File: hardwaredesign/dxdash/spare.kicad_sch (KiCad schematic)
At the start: 0 parts

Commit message: added screw terminals
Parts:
- added J10, J11, J3, J7, J9: Screw_Terminal_01x04, TerminalBlock_Phoenix:TerminalBlock_Phoenix_MKDS-3-4-5.08_1x04_P5.08mm_Horizontal, symbol Connector:Screw_Terminal_01x04
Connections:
- new net 24V: J3.1 (Pin_1)
- new net CANH: J9.1 (Pin_1)
- new net CANL: J9.2 (Pin_2)
- new net GND: J10.1 (Pin_1), J3.2 (Pin_2)
- new net OUT1_LS: J3.3 (Pin_3)
- new net OUT2_LS: J3.4 (Pin_4)
- new net OUT3_LS: J7.1 (Pin_1)
- new net button1: J11.1 (Pin_1)
- new net button2: J11.2 (Pin_2)
- new net button3: J11.3 (Pin_3)
- new net button4: J11.4 (Pin_4)
- new net pot1: J10.2 (Pin_2)
- new net pot2: J10.3 (Pin_3)
- new net pot5V: J10.4 (Pin_4)
- no-connect marks 0 -> 5

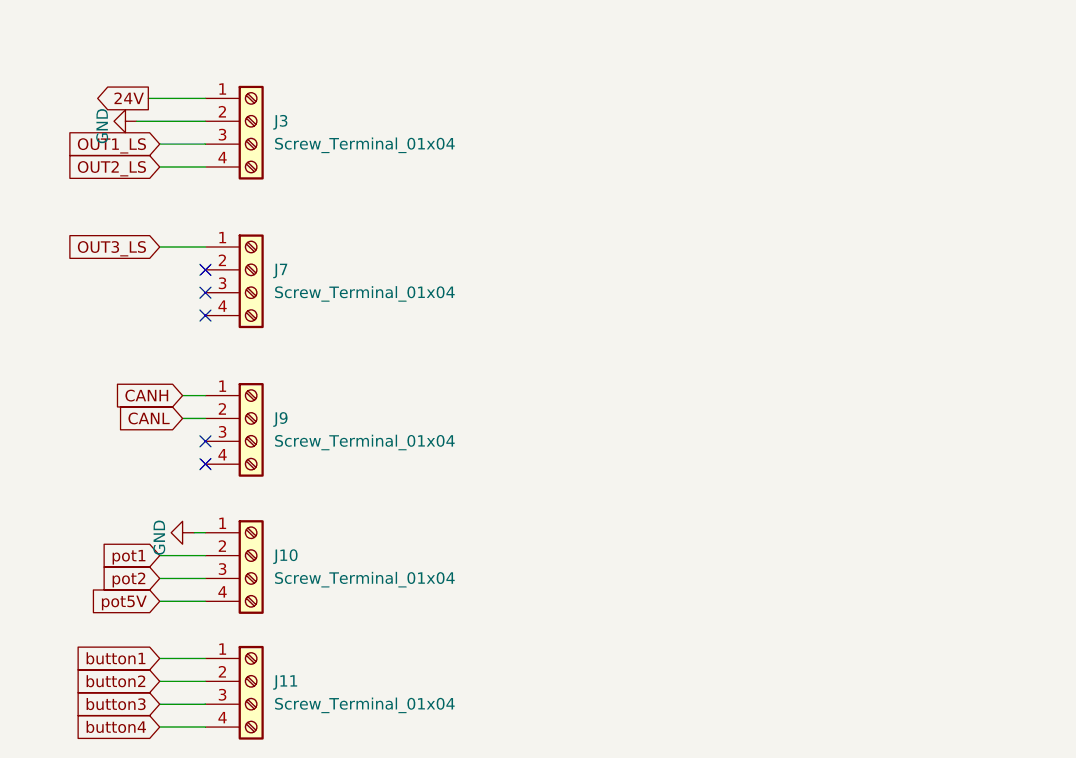
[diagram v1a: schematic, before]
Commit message: added switch inputs. Layout preparation.
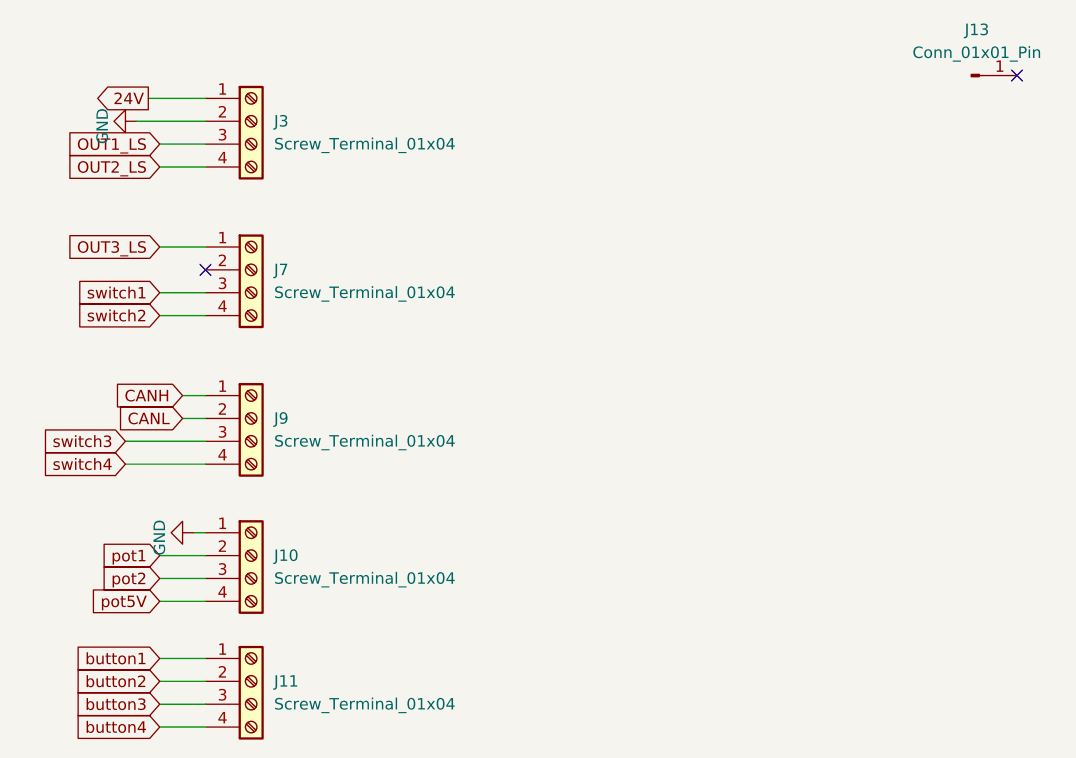
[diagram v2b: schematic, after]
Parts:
- added J13: Conn_01x01_Pin, Connector_PinHeader_2.54mm:PinHeader_1x01_P2.54mm_Vertical, symbol Connector:Conn_01x01_Pin
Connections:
- net switch1: now reaches J7.3 (Pin_3)
- net switch2: now reaches J7.4 (Pin_4)
- net switch3: now reaches J9.3 (Pin_3)
- net switch4: now reaches J9.4 (Pin_4)
- no-connect marks 5 -> 2
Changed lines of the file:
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@@
 	(paper "A4")
 	(no_connect
-		(at 77.47 85.09)
-	)
-	(no_connect
-		(at 77.47 66.04)
+		(at 167.64 41.91)
 	)
 	(no_connect
 		(at 77.47 63.5)
 	)
-	(no_connect
-		(at 77.47 68.58)
-	)
-	(no_connect
-		(at 77.47 82.55)
-	)
 	(wire
 		(pts
@@
 	(wire
 		(pts
+			(xy 68.58 82.55) (xy 77.47 82.55)
+		)
+		(stroke
+			(width 0)
+			(type default)
+		)
+	)
+	(wire
+		(pts
 			(xy 72.39 95.25) (xy 77.47 95.25)
 		)
@@
 	(wire
 		(pts
+			(xy 68.58 85.09) (xy 77.47 85.09)
+		)
+		(stroke
+			(width 0)
+			(type default)
+		)
+	)
+	(wire
+		(pts
+			(xy 72.39 68.58) (xy 77.47 68.58)
+		)
+		(stroke
+			(width 0)
+			(type default)
+		)
+	)
+	(wire
+		(pts
 			(xy 74.93 80.01) (xy 77.47 80.01)
 		)
@@
 		(pts
 			(xy 77.47 60.96) (xy 72.39 60.96)
+		)
+		(stroke
+			(width 0)
+			(type default)
+		)
+	)
+	(wire
+		(pts
+			(xy 72.39 66.04) (xy 77.47 66.04)
 		)
 		(stroke
@@
 		)
 	)
+	(global_label "switch4"
+		(shape input)
+		(at 68.58 85.09 180)
+		(fields_autoplaced yes)
+		(effects
+			(font
+				(size 1.27 1.27)
+			)
+			(justify right)
+		)
+		(property "Intersheetrefs" "${INTERSHEET_REFS}"
+			(at 58.4586 85.09 0)
+			(effects
+				(font
+					(size 1.27 1.27)
+				)
+				(justify right)
+				(hide yes)
+			)
+		)
+	)
 	(global_label "button2"
 		(shape input)
@@
 		)
 	)
+	(global_label "switch1"
+		(shape input)
+		(at 72.39 66.04 180)
+		(fields_autoplaced yes)
+		(effects
+			(font
+				(size 1.27 1.27)
+			)
+			(justify right)
+		)
+		(property "Intersheetrefs" "${INTERSHEET_REFS}"
+			(at 62.2686 66.04 0)
+			(effects
+				(font
+					(size 1.27 1.27)
+				)
+				(justify right)
+				(hide yes)
+			)
+		)
+	)
 	(global_label "OUT1_LS"
 		(shape input)
@@
 		(property "Intersheetrefs" "${INTERSHEET_REFS}"
 			(at 65.1716 97.79 0)
+			(effects
+				(font
+					(size 1.27 1.27)
+				)
+				(justify right)
+				(hide yes)
+			)
+		)
+	)
+	(global_label "switch3"
+		(shape input)
+		(at 68.58 82.55 180)
+		(fields_autoplaced yes)
+		(effects
+			(font
+				(size 1.27 1.27)
+			)
+			(justify right)
+		)
+		(property "Intersheetrefs" "${INTERSHEET_REFS}"
+			(at 58.4586 82.55 0)
+			(effects
+				(font
+					(size 1.27 1.27)
+				)
+				(justify right)
+				(hide yes)
+			)
+		)
+	)
+	(global_label "switch2"
+		(shape input)
+		(at 72.39 68.58 180)
+		(fields_autoplaced yes)
+		(effects
+			(font
+				(size 1.27 1.27)
+			)
+			(justify right)
+		)
+		(property "Intersheetrefs" "${INTERSHEET_REFS}"
+			(at 62.2686 68.58 0)
 			(effects
 				(font
@@
 					(unit 1)
 				)
+			)
+		)
+	)
+	(symbol
+		(lib_id "Connector:Conn_01x01_Pin")
+		(at 162.56 41.91 0)
+		(unit 1)
+		(exclude_from_sim no)
+		(in_bom yes)
+		(on_board yes)
+		(dnp no)
+		(fields_autoplaced yes)
+		(property "Reference" "J13"
+			(at 163.195 36.83 0)
+			(effects
+				(font
+					(size 1.27 1.27)
+				)
+			)
+		)
+		(property "Value" "Conn_01x01_Pin"
+			(at 163.195 39.37 0)
+			(effects
+				(font
+					(size 1.27 1.27)
+				)
+			)
+		)
+		(property "Footprint" "Connector_PinHeader_2.54mm:PinHeader_1x01_P2.54mm_Vertical"
+			(at 162.56 41.91 0)
+			(effects
+				(font
+					(size 1.27 1.27)
+				)
+				(hide yes)
+			)
+		)
+		(property "Datasheet" "~"
+			(at 162.56 41.91 0)
+			(effects
+				(font
+					(size 1.27 1.27)
+				)
+				(hide yes)
+			)
+		)
+		(property "Description" "Generic connector, single row, 01x01, script generated"
+			(at 162.56 41.91 0)
+			(effects
+				(font
+					(size 1.27 1.27)
+				)
+				(hide yes)
+			)
+		)
+		(pin "1"
+		)
+		(instances
+			(project ""
+				(path "/e63e39d7-6ac0-4ffd-8aa3-1841a4541b55/5f264cb2-d509-40cd-8689-92eb5ea24d84"
+					(reference "J13")
+					(unit 1)
+				)

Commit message: more layout
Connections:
- net CANH: now also J9.3 (Pin_3); no longer J9.1 (Pin_1)
- net OUT3_LS: now also J9.1 (Pin_1); no longer J7.1 (Pin_1)
- net switch1: now also J7.1 (Pin_1); no longer J7.3 (Pin_3)
- net switch2: now also J7.2 (Pin_2); no longer J7.4 (Pin_4)
- net switch3: now also J7.3 (Pin_3); no longer J9.3 (Pin_3)
- net switch4: now also J7.4 (Pin_4); no longer J9.4 (Pin_4)
